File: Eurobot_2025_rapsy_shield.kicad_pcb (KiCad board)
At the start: 2 copper layers, 56 x 65 mm, 30 parts, among them J1 Raspberry_Pi_2_3, J2 SPI, J4 Conn_01x02, J5 AU, J6 Conn_01x04, Q1 2N7002, Q2 2N7002, U1 TPS54302

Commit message: v1 ok
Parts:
- added C_Act1: Conn_02x05_Odd_Even, Connector_IDC:IDC-Header_2x05_P2.54mm_Vertical, F.Cu at (54.7, 54.2)
- added C_Act2: Conn_02x05_Odd_Even, Connector_IDC:IDC-Header_2x05_P2.54mm_Vertical, F.Cu at (54.6, 31.6)
- moved J2 20.5 mm to (31.0, 39.9), turned to -90 degrees
- moved R6 4.81 mm to (33.9, 53.7)
- moved R5 3.60 mm to (31.2, 55.3)
- moved J5 1.32 mm to (37.7, 51.6)
- moved J1 0.20 mm to (24.5, 76.7)
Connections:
- J1 pad 11: unconnected-(J1-GPIO17-Pad11) -> C_Act1-3
- J1 pad 12: unconnected-(J1-GPIO18/PWM0-Pad12) -> C_Act1-9
- J1 pad 13: unconnected-(J1-GPIO27-Pad13) -> C_Act1-2
- J1 pad 15: unconnected-(J1-GPIO22-Pad15) -> C_Act1-4
- J1 pad 16: unconnected-(J1-GPIO23-Pad16) -> C_Act1-6
- J1 pad 22: unconnected-(J1-GPIO25-Pad22) -> C_Act1-8
- J1 pad 29: unconnected-(J1-GCLK1/GPIO5-Pad29) -> C_Act2-8
- J1 pad 3: unconnected-(J1-SDA/GPIO2-Pad3) -> C_Act1-1
- J1 pad 31: unconnected-(J1-GCLK2/GPIO6-Pad31) -> C_Act2-4
- J1 pad 32: unconnected-(J1-PWM0/GPIO12-Pad32) -> C_Act2-2
- J1 pad 33: unconnected-(J1-PWM1/GPIO13-Pad33) -> C_Act2-6
- J1 pad 35: unconnected-(J1-GPIO19/MISO1-Pad35) -> C_Act2-7
- J1 pad 36: unconnected-(J1-GPIO16-Pad36) -> C_Act2-1
- J1 pad 37: unconnected-(J1-GPIO26-Pad37) -> C_Act2-5
- J1 pad 38: unconnected-(J1-GPIO20/MOSI1-Pad38) -> C_Act2-9
- J1 pad 40: unconnected-(J1-GPIO21/SCLK1-Pad40) -> C_Act2-3
- J1 pad 5: unconnected-(J1-SCL/GPIO3-Pad5) -> C_Act1-5
- J1 pad 7: unconnected-(J1-GCLK0/GPIO4-Pad7) -> C_Act1-7
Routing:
- net C_Act1-9: track 0.00 -> 37.5 mm, vias 0 -> 2
- net C_Act1-1: track 0.00 -> 36.9 mm
- net C_Act1-8: track 0.00 -> 36.6 mm, vias 0 -> 1
- net C_Act2-3: track 0.00 -> 36.5 mm
- net C_Act1-2: track 0.00 -> 35.9 mm, vias 0 -> 2
- net C_Act1-7: track 0.00 -> 35.7 mm
- net C_Act1-4: track 0.00 -> 34.6 mm
- net C_Act1-6: track 0.00 -> 34.6 mm
- net C_Act2-4: track 0.00 -> 34.2 mm
- net C_Act2-7: track 0.00 -> 34.1 mm
- net C_Act2-6: track 0.00 -> 34.0 mm
- net C_Act2-9: track 0.00 -> 34.0 mm
- net C_Act2-1: track 0.00 -> 34.0 mm
- net C_Act2-2: track 0.00 -> 33.9 mm
- net C_Act1-3: track 0.00 -> 33.7 mm, vias 0 -> 2
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- added copper zone on B.Cu, net 3.3V
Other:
- board text added: "AU"
- board text added: "ROS c'est de la merde mais on l'utilise au cas ou"
- board text added: "SPI"
- board text added: "UART"
- board text added: "Vin = 24V"
- board text added: "shield raspberry pi 4 opossums 2024"

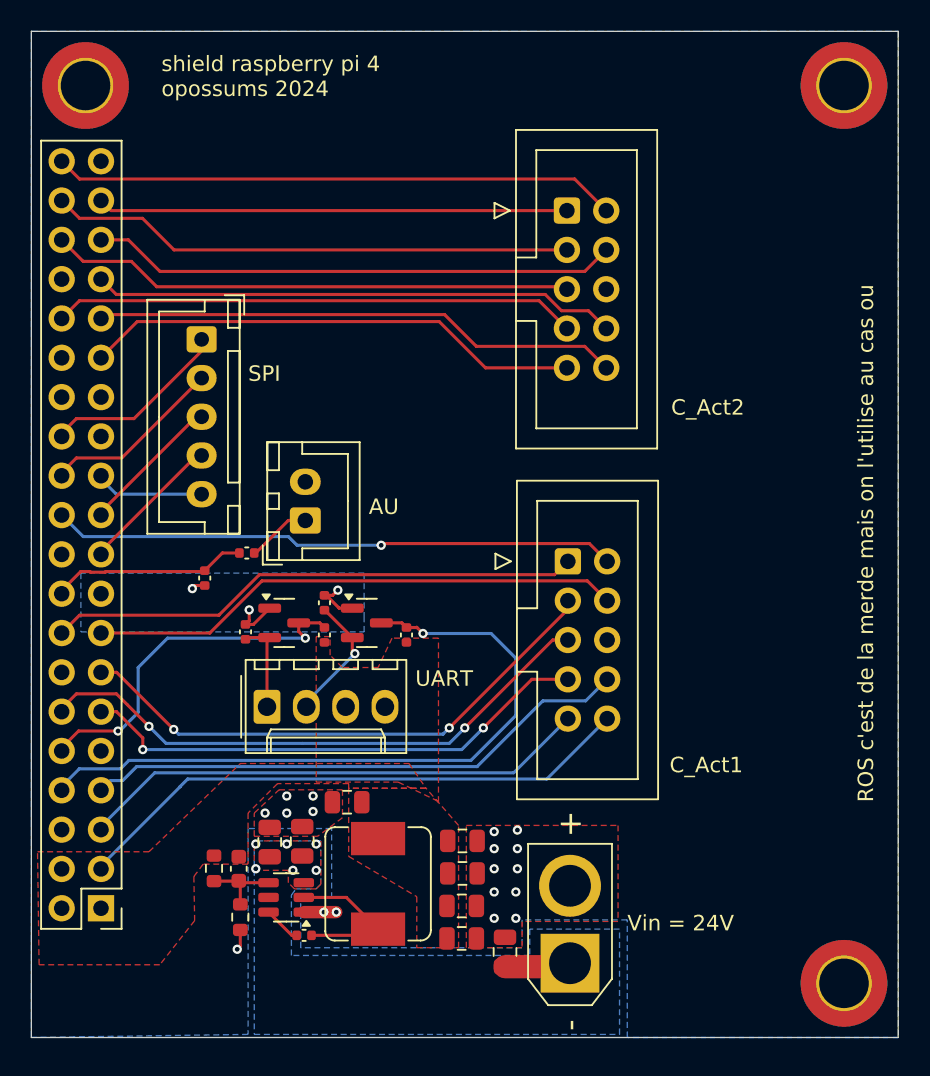
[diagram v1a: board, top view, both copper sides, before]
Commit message: schematic for can
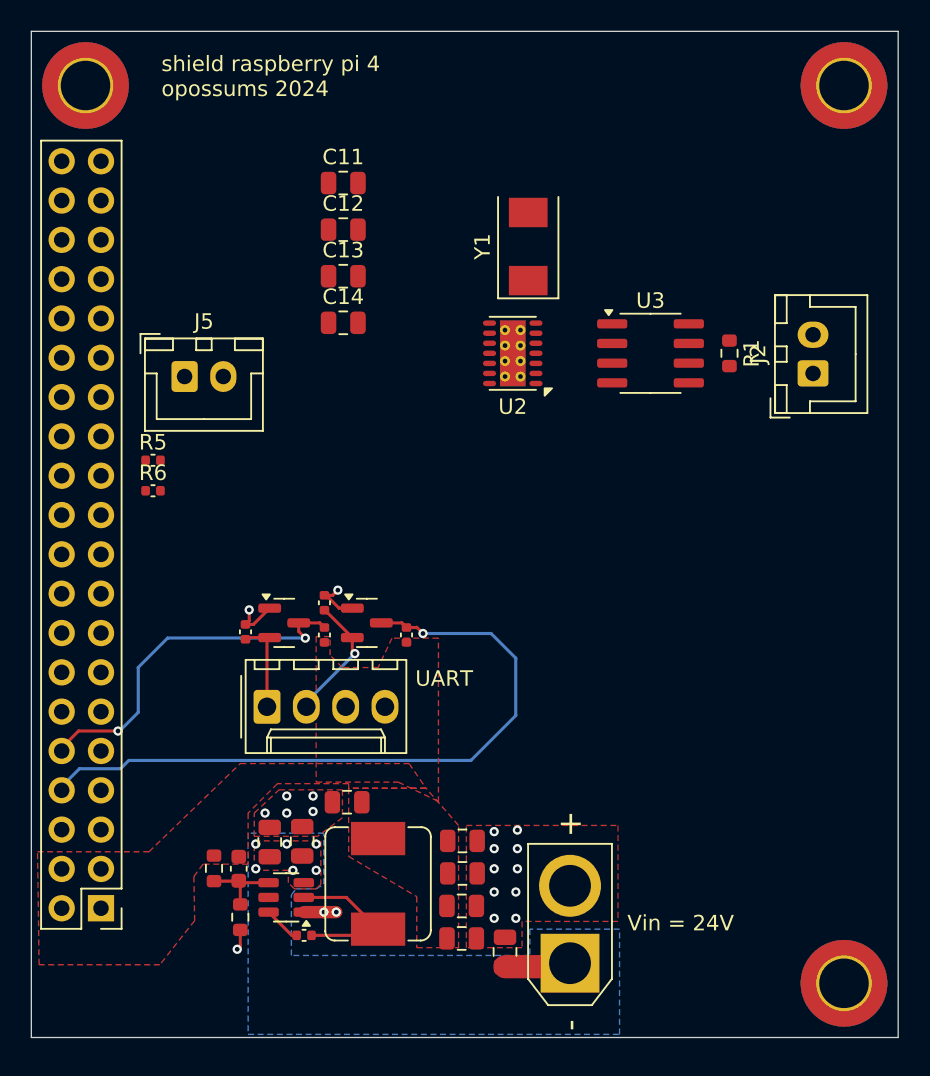
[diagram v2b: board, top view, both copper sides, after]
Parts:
- removed C_Act1, C_Act2: Conn_02x05_Odd_Even, Connector_IDC:IDC-Header_2x05_P2.54mm_Vertical
- added C11: 0.1uF 10V, Capacitor_SMD:C_0805_2012Metric, F.Cu at (40.1, 29.8)
- added C12: 22pF, Capacitor_SMD:C_0805_2012Metric, F.Cu at (40.1, 32.8)
- added C13: 22pF, Capacitor_SMD:C_0805_2012Metric, F.Cu at (40.1, 35.8)
- added C14: 0.1uF, Capacitor_SMD:C_0805_2012Metric, F.Cu at (40.1, 38.8)
- added R1: 120R, Resistor_SMD:R_0603_1608Metric, F.Cu at (65.1, 40.8)
- added U2: MCP2518FD-xQBB, Package_DFN_QFN:DFN-14-1EP_3x4.5mm_P0.65mm_EP1.65x4.25mm_ThermalVias, F.Cu at (51.1, 40.8)
- added U3: ATA6563, Package_SO:SOIC-8_3.9x4.9mm_P1.27mm, F.Cu at (60.0, 40.8)
- added Y1: 20MHz, Crystal:Crystal_SMD_0603-2Pin_6.0x3.5mm, F.Cu at (52.1, 33.9)
- C1, C2: value 22µF 25V -> 10µF 50V
- C3: value 22µF 25V -> 100nF 50V
- C4: value 220nF 16V -> 100nF 50V
- J2: value SPI -> CAN; footprint Connector_JST:JST_XH_B5B-XH-A_1x05_P2.50mm_Vertical -> Connector_JST:JST_XH_B2B-XH-A_1x02_P2.50mm_Vertical
- R3: value 68k -> 100k
- R4: value 9.1k -> 13.3k
- moved J2 39.6 mm to (70.5, 42.1), turned to 90 degrees
- moved J5 12.1 mm to (29.9, 42.3), turned to 0 degrees
- moved R5 8.31 mm to (27.9, 47.7), turned to 0 degrees
- moved R6 7.27 mm to (27.9, 49.7), turned to 0 degrees
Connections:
- J1 pad 1: (no net) -> 3.3V
- J1 pad 11: C_Act1-3 -> unconnected-(J1-GPIO17-Pad11)
- J1 pad 12: C_Act1-9 -> unconnected-(J1-GPIO18/PWM0-Pad12)
- J1 pad 13: C_Act1-2 -> unconnected-(J1-GPIO27-Pad13)
- J1 pad 15: C_Act1-4 -> unconnected-(J1-GPIO22-Pad15)
- J1 pad 16: C_Act1-6 -> unconnected-(J1-GPIO23-Pad16)
- J1 pad 22: C_Act1-8 -> unconnected-(J1-GPIO25-Pad22)
- J1 pad 29: C_Act2-8 -> unconnected-(J1-GCLK1/GPIO5-Pad29)
- J1 pad 3: C_Act1-1 -> unconnected-(J1-SDA/GPIO2-Pad3)
- J1 pad 31: C_Act2-4 -> unconnected-(J1-GCLK2/GPIO6-Pad31)
- J1 pad 32: C_Act2-2 -> unconnected-(J1-PWM0/GPIO12-Pad32)
- J1 pad 33: C_Act2-6 -> unconnected-(J1-PWM1/GPIO13-Pad33)
- J1 pad 35: C_Act2-7 -> unconnected-(J1-GPIO19/MISO1-Pad35)
- J1 pad 36: C_Act2-1 -> unconnected-(J1-GPIO16-Pad36)
- J1 pad 37: C_Act2-5 -> unconnected-(J1-GPIO26-Pad37)
- J1 pad 38: C_Act2-9 -> unconnected-(J1-GPIO20/MOSI1-Pad38)
- J1 pad 40: C_Act2-3 -> unconnected-(J1-GPIO21/SCLK1-Pad40)
- J1 pad 5: C_Act1-5 -> unconnected-(J1-SCL/GPIO3-Pad5)
- J1 pad 7: C_Act1-7 -> unconnected-(J1-GCLK0/GPIO4-Pad7)
- J2 pad 1: CE1 -> Net-(J2-Pin_1)
- J2 pad 2: CE0 -> Net-(J2-Pin_2)
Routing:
- net C_Act1-9: track 37.5 -> 0.00 mm, vias 2 -> 0
- net C_Act1-1: track 36.9 -> 0.00 mm
- net C_Act1-8: track 36.6 -> 0.00 mm, vias 1 -> 0
- net C_Act2-3: track 36.5 -> 0.00 mm
- net C_Act1-2: track 35.9 -> 0.00 mm, vias 2 -> 0
- net C_Act1-7: track 35.7 -> 0.00 mm
- net C_Act1-4: track 34.6 -> 0.00 mm
- net C_Act1-6: track 34.6 -> 0.00 mm
- net C_Act2-4: track 34.2 -> 0.00 mm
- net C_Act2-7: track 34.1 -> 0.00 mm
- net C_Act2-6: track 34.0 -> 0.00 mm
- net C_Act2-9: track 34.0 -> 0.00 mm
- net C_Act2-1: track 34.0 -> 0.00 mm
- net C_Act2-2: track 33.9 -> 0.00 mm
- net C_Act1-3: track 33.7 -> 0.00 mm, vias 2 -> 0
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- removed copper zone on B.Cu, net 3.3V
- removed copper zone on B.Cu, net GND
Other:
- board text removed: "AU"
- board text removed: "ROS c'est de la merde mais on l'utilise au cas ou"
- board text removed: "SPI"
